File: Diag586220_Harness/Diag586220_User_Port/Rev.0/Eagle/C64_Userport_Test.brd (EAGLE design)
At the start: 53 x 55 mm, 20 parts, among them IC1 4066N, IC2 4066N, J1 C64-USERPORT

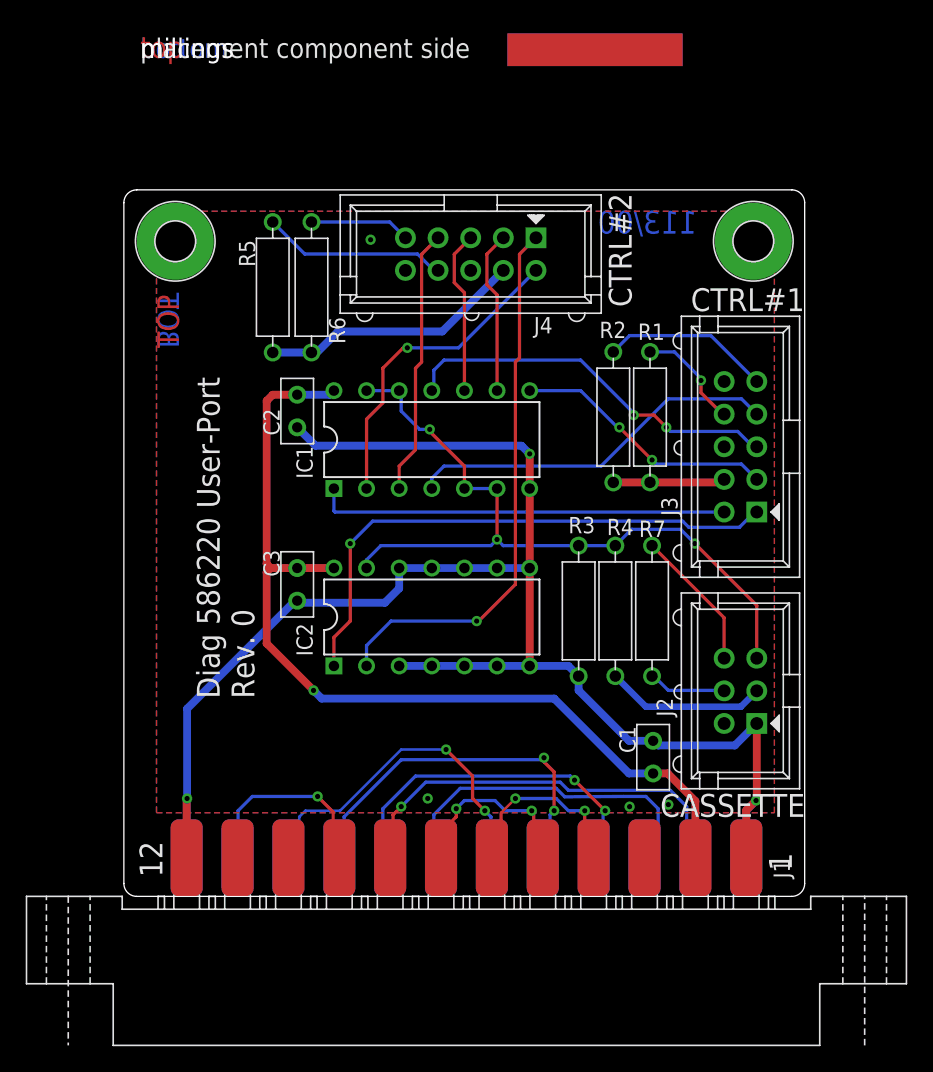
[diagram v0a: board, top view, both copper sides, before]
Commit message: Add files via upload
values from 120k to 110k and 320R to 316R
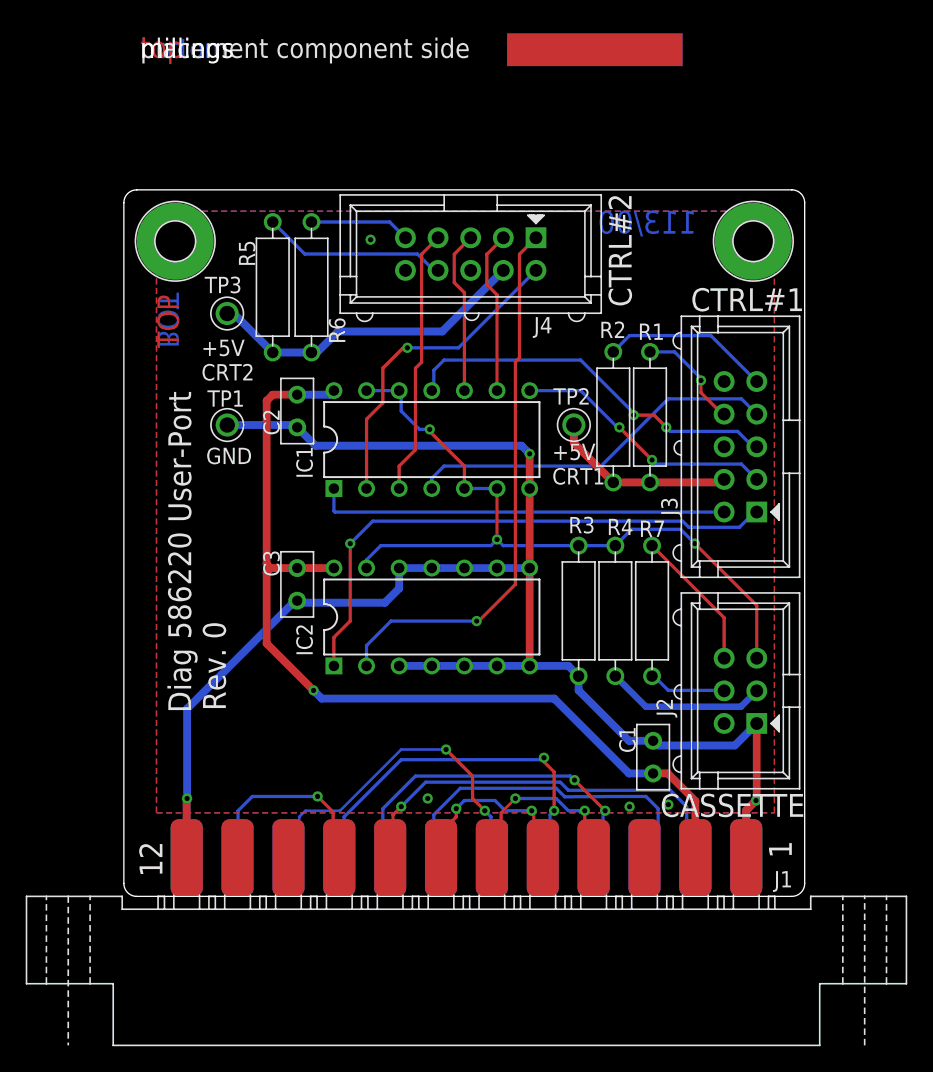
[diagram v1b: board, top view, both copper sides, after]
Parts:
- added TP1, TP2, TP3: L1,2_R, Pads:1,2MM_R
- R1, R2, R5, R6: value 120k -> 110k
- R3: value 320R -> 316R
- renumbered BHR1 to DRL1, BHR2 to DRL2
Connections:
- net +5VCTR1: now also TP2.1
- net +5VCTR2: now also TP3.1
- net GND: now also TP1.1
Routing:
- net +5VCTR1: track 8.73 -> 14.5 mm
- net GND: track 131.6 -> 137.1 mm
- net +5VCTR2: track 20.6 -> 25.4 mm
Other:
- board text added: "+5V CRT1"
- board text added: "+5V CRT2"
- board text added: "GND"
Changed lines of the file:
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@@
 <?xml version="1.0" encoding="utf-8"?>
 <!DOCTYPE eagle SYSTEM "eagle.dtd">
-<eagle version="9.2.2">
+<eagle version="9.5.2">
 <drawing>
 <settings>
@@
 <setting verticaltext="up"/>
 </settings>
-<grid distance="0.5" unitdist="mm" unit="mm" style="lines" multiple="16" display="yes" altdistance="5" altunitdist="mil" altunit="mil"/>
+<grid distance="6.25" unitdist="mil" unit="mil" style="lines" multiple="16" display="yes" altdistance="5" altunitdist="mil" altunit="mil"/>
 <layers>
 <layer number="1" name="Top" color="4" fill="1" visible="yes" active="yes"/>
@@
 <layer number="28" name="bValues" color="7" fill="1" visible="no" active="yes"/>
 <layer number="29" name="tStop" color="7" fill="3" visible="no" active="yes"/>
-<layer number="30" name="bStop" color="7" fill="6" visible="yes" active="yes"/>
+<layer number="30" name="bStop" color="7" fill="6" visible="no" active="yes"/>
 <layer number="31" name="tCream" color="7" fill="4" visible="no" active="yes"/>
 <layer number="32" name="bCream" color="7" fill="5" visible="no" active="yes"/>
@@
 <layer number="45" name="Holes" color="7" fill="1" visible="no" active="yes"/>
 <layer number="46" name="Milling" color="3" fill="1" visible="no" active="yes"/>
-<layer number="47" name="Measures" color="7" fill="1" visible="no" active="yes"/>
+<layer number="47" name="Measures" color="7" fill="1" visible="yes" active="yes"/>
 <layer number="48" name="Document" color="7" fill="1" visible="yes" active="yes"/>
 <layer number="49" name="Reference" color="7" fill="1" visible="yes" active="yes"/>
@@
 <wire x1="1" y1="0" x2="52" y2="0" width="0" layer="20"/>
 <wire x1="52" y1="0" x2="53" y2="1" width="0" layer="20" curve="90"/>
-<text x="7.46125" y="15.39875" size="1.778" layer="21" rot="R90">Diag 586220 User-Port</text>
-<text x="10.16" y="15.39875" size="1.778" layer="21" rot="R90">Rev. 0</text>
+<text x="5.23875" y="14.2875" size="1.778" layer="21" rot="R90">Diag 586220 User-Port</text>
+<text x="7.9375" y="14.44625" size="1.778" layer="21" rot="R90">Rev. 0</text>
 <text x="41.75125" y="6.19125" size="1.778" layer="21">CASSETTE</text>
 <text x="44.1325" y="45.56125" size="1.778" layer="21">CTRL#1</text>
@@
 <text x="1.5" y="74.5" size="1.778" layer="48">Diag 586220
 Harness</text>
-<text x="52" y="2" size="1.778" layer="21" rot="R90">1</text>
+<text x="52" y="2.9525" size="1.778" layer="21" rot="SR90">1</text>
 <text x="3" y="1.5" size="1.778" layer="21" rot="R90">12</text>
+<text x="6.39625" y="33.65375" size="1.27" layer="21">GND</text>
+<text x="6.0325" y="40.16375" size="1.27" layer="21">+5V
+CRT2</text>
+<text x="33.3375" y="32.0675" size="1.27" layer="21">+5V
+CRT1</text>
 </plain>
 <attributes>
@@
 </element>
 <element name="J1" library="Commodore" package="USERPORT" value="C64-USERPORT" x="26.67" y="0" smashed="yes" rot="R180">
-<attribute name="NAME" x="51.8475" y="1.40125" size="1.27" layer="25" rot="R90"/>
+<attribute name="NAME" x="50.61375" y="0.69875" size="1.27" layer="25"/>
 <attribute name="VALUE" x="50.67" y="-3" size="1.27" layer="27" rot="R180"/>
 </element>
@@
 <attribute name="NAME" x="31.91495" y="43.8275" size="1.27" layer="25"/>
 </element>
-<element name="R1" library="DISCRETE" package="R-10" value="120k" x="40.9575" y="37.30625" smashed="yes" rot="R270">
+<element name="R1" library="DISCRETE" package="R-10" value="110k" x="40.9575" y="37.30625" smashed="yes" rot="R270">
 <attribute name="NAME" x="40.01875" y="43.3225" size="1.27" layer="25"/>
 <attribute name="VALUE" x="40.3225" y="40.48125" size="1.27" layer="27" rot="R270"/>
 </element>
-<element name="R2" library="DISCRETE" package="R-10" value="120k" x="38.1" y="37.30625" smashed="yes" rot="R270">
+<element name="R2" library="DISCRETE" package="R-10" value="110k" x="38.1" y="37.30625" smashed="yes" rot="R270">
 <attribute name="NAME" x="37.01875" y="43.465" size="1.27" layer="25"/>
 <attribute name="VALUE" x="37.465" y="40.48125" size="1.27" layer="27" rot="R270"/>
 </element>
-<element name="R3" library="DISCRETE" package="R-10" value="320R" x="35.40125" y="22.225" smashed="yes" rot="R270">
+<element name="R3" library="DISCRETE" package="R-10" value="316R" x="35.40125" y="22.225" smashed="yes" rot="R270">
 <attribute name="NAME" x="34.6" y="28.26625" size="1.27" layer="25"/>
 <attribute name="VALUE" x="34.76625" y="25.4" size="1.27" layer="27" rot="R270"/>
@@
 <attribute name="VALUE" x="37.62375" y="25.4" size="1.27" layer="27" rot="R270"/>
 </element>
-<element name="R5" library="DISCRETE" package="R-10" value="120k" x="11.58875" y="47.41875" smashed="yes" rot="R270">
+<element name="R5" library="DISCRETE" package="R-10" value="110k" x="11.58875" y="47.41875" smashed="yes" rot="R270">
 <attribute name="NAME" x="8.95375" y="51.09375" size="1.27" layer="25" rot="R270"/>
 <attribute name="VALUE" x="10.95375" y="50.59375" size="1.27" layer="27" rot="R270"/>
 </element>
-<element name="R6" library="DISCRETE" package="R-10" value="120k" x="14.605" y="47.41875" smashed="yes" rot="R270">
+<element name="R6" library="DISCRETE" package="R-10" value="110k" x="14.605" y="47.41875" smashed="yes" rot="R270">
 <attribute name="NAME" x="15.97" y="45.09375" size="1.27" layer="25" rot="R270"/>
 <attribute name="VALUE" x="13.97" y="50.59375" size="1.27" layer="27" rot="R270"/>
@@
 </element>
 <element name="U$17" library="I-TEILE" package="2LAYER" value="" x="4.28625" y="42.70375" smashed="yes" rot="R90"/>
-<element name="BHR1" library="Mech_Bohr" package="BOHR3,2" value="" x="4" y="51" smashed="yes"/>
-<element name="BHR2" library="Mech_Bohr" package="BOHR3,2" value="" x="49" y="51" smashed="yes"/>
+<element name="DRL1" library="Mech_Bohr" package="BOHR3,2" value="" x="4" y="51" smashed="yes"/>
+<element name="DRL2" library="Mech_Bohr" package="BOHR3,2" value="" x="49" y="51" smashed="yes"/>
 <element name="U$18" library="DOC_IBSP" package="PCB-TITLE/" value="" x="0" y="64" smashed="yes">
 <attribute name="DRAWING_NAME" x="1.27" y="70.985" size="1.6764" layer="48" font="vector" ratio="12"/>
 <attribute name="LAST_DATE_TIME" x="1.27" y="67.81" size="1.6764" layer="48" font="vector" ratio="12"/>
+</element>
+<element name="TP1" library="Pads" package="1,2MM_R" value="L1,2_R" x="8.0475" y="36.69375" smashed="yes">
+<attribute name="NAME" x="6.5075" y="38.1225" size="1.27" layer="25"/>
+</element>
+<element name="TP2" library="Pads" package="1,2MM_R" value="L1,2_R" x="35.02875" y="36.6975" smashed="yes">
+<attribute name="NAME" x="33.44125" y="38.285" size="1.27" layer="25"/>
+</element>
+<element name="TP3" library="Pads" package="1,2MM_R" value="L1,2_R" x="8.04125" y="45.37375" smashed="yes">
+<attribute name="NAME" x="6.295" y="46.96125" size="1.27" layer="25"/>
 </element>
 </elements>
@@
 <via x="39.37" y="6.985" extent="1-16" drill="0.4"/>
 <via x="23.65375" y="7.62" extent="1-16" drill="0.4"/>
+<contactref element="TP1" pad="1"/>
+<wire x1="8.0475" y1="36.69375" x2="13.3125" y2="36.69375" width="0.6096" layer="16"/>
+<wire x1="13.3125" y1="36.69375" x2="13.49375" y2="36.5125" width="0.6096" layer="16"/>
 </signal>
 <signal name="+5V">
@@
 <wire x1="46.49625" y1="32.22625" x2="40.9575" y2="32.22625" width="0.6096" layer="1"/>
 <wire x1="40.9575" y1="32.22625" x2="38.1" y2="32.22625" width="0.6096" layer="1"/>
+<contactref element="TP2" pad="1"/>
+<wire x1="38.1" y1="32.22625" x2="35.02875" y2="35.2975" width="0.6096" layer="1"/>
+<wire x1="35.02875" y1="35.2975" x2="35.02875" y2="36.6975" width="0.6096" layer="1"/>
 </signal>
 <signal name="POTXA">
@@
 <wire x1="16.66875" y1="43.97375" x2="24.78375" y2="43.97375" width="0.6096" layer="16"/>
 <wire x1="24.78375" y1="43.97375" x2="29.54" y2="48.73" width="0.6096" layer="16"/>
+<contactref element="TP3" pad="1"/>
+<wire x1="8.04125" y1="45.37375" x2="8.55375" y2="45.37375" width="0.6096" layer="16"/>
+<wire x1="8.55375" y1="45.37375" x2="11.58875" y2="42.33875" width="0.6096" layer="16"/>
 </signal>
 </signals>
